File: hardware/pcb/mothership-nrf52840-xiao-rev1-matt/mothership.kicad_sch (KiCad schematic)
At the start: 42 parts, among them J1 HRO TYPE-C-31-M-12, J10 CONN_BATT, J11 Screw_Terminal_ADB_VCC, J2 USB_EXT_FFC_CABLE, J3 Screw_Terminal_ADB_SHIELD, J4 CONN_MATRIX_BOT_L, J5 CONN_MATRIX_BOT_R, J6 CONN_MATRIX_TOP_R, J7 CONN_MATRIX_TOP_L, J8 SPI, J9 EC11, Q1 AO3401A, Q2 FDC6305N, SW1 SW_SPDT_321, SW2 SW_SPST, U1 NCP361SN, U2 XIAO_nRF52840, U3 MCP23017x-x-SS, U4 MCP23017x-x-SS, U5 DT1452-02SO, U6 HY2115-LB9D

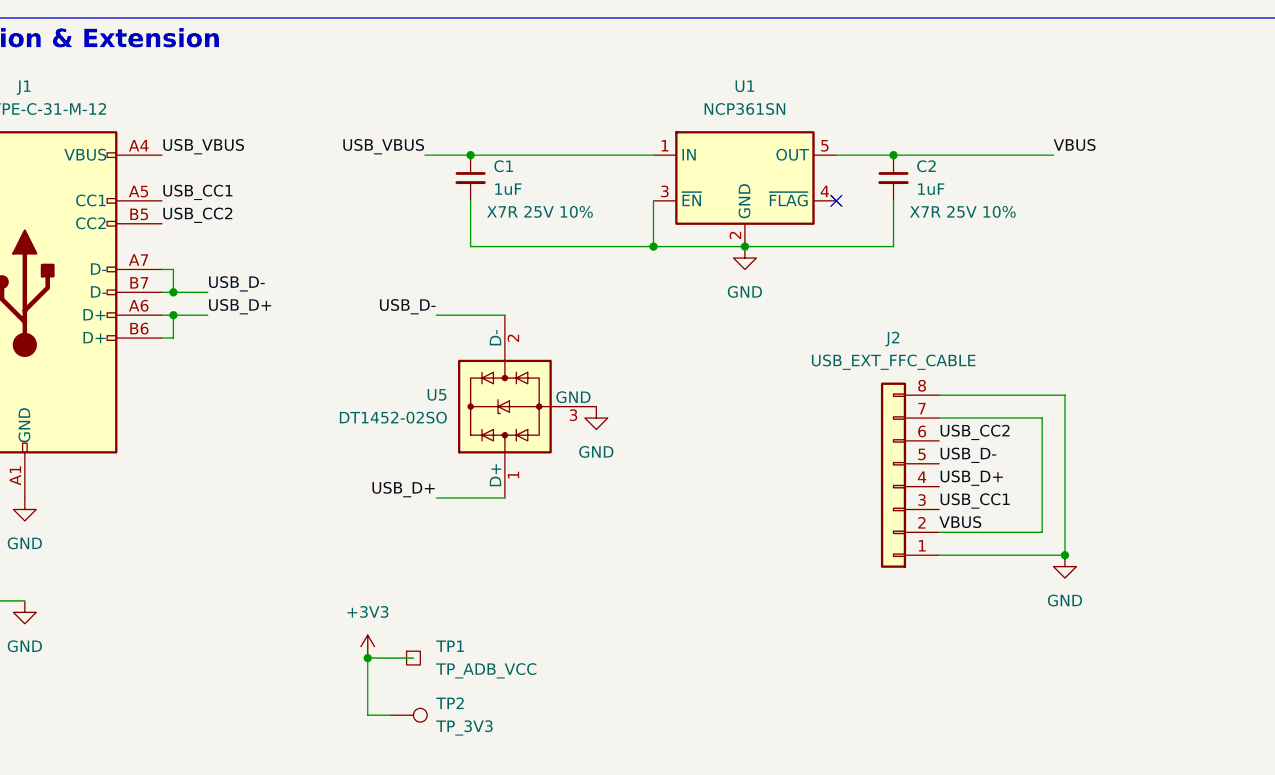
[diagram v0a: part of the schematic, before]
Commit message: sch: switch to use 4P flex adapter + 5.1k for CC lines
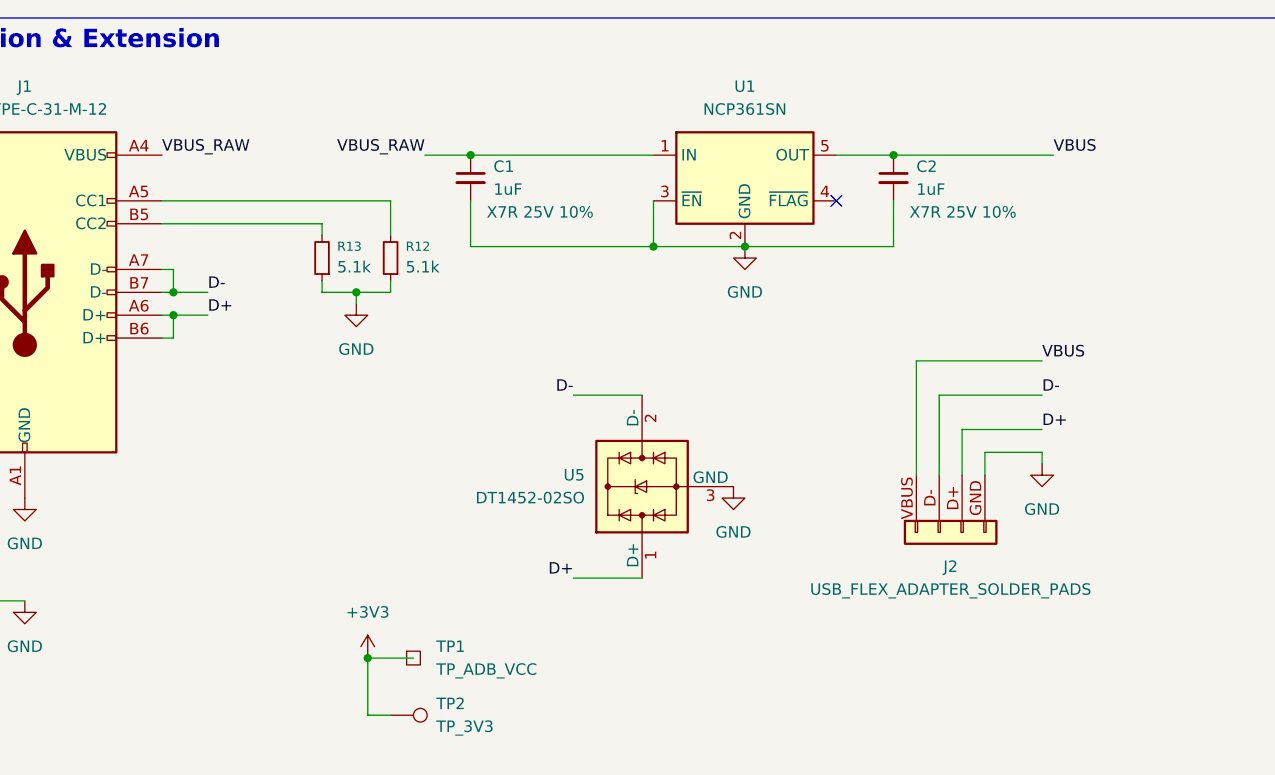
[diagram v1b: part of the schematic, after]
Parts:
- added R12, R13: 5.1k, A9M0330:Resistor_SMD__R_0603_1608Metric_Pad0.98x0.95mm_HandSolder, symbol A9M0330:R_Small
- J2: value USB_EXT_FFC_CABLE -> USB_FLEX_ADAPTER_SOLDER_PADS; symbol A9M0330:Conn_01x08 -> A9M0330:Conn_01x04_USB_FFC
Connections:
- net GND: now also J2.GND, R12.1, R13.1; no longer J2.1 (Pin_1), J2.8 (Pin_8)
- net USB_VBUS: no longer C1.1, J1.A4 (VBUS), J1.A9 (VBUS), J1.B4 (VBUS), J1.B9 (VBUS), U1.1 (IN)
- net VBUS: now also J2.VBUS; no longer J2.2 (Pin_2), J2.7 (Pin_7)
- net USB_CC1: no longer names the net of J1.A5 (CC1)
- net USB_CC1: now also R12.2; no longer J2.3 (Pin_3)
- net USB_CC2: no longer names the net of J1.B5 (CC2)
- net USB_CC2: now also R13.2; no longer J2.6 (Pin_6)
- net USB_D+ renamed D+
- net D+: now also J2.D+; no longer J2.4 (Pin_4)
- net USB_D- renamed D-
- net D-: now also J2.D-; no longer J2.5 (Pin_5)
- new net VBUS_RAW: C1.1, J1.A4 (VBUS), J1.A9 (VBUS), J1.B4 (VBUS), J1.B9 (VBUS), U1.1 (IN)
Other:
- moved on the sheet: U5

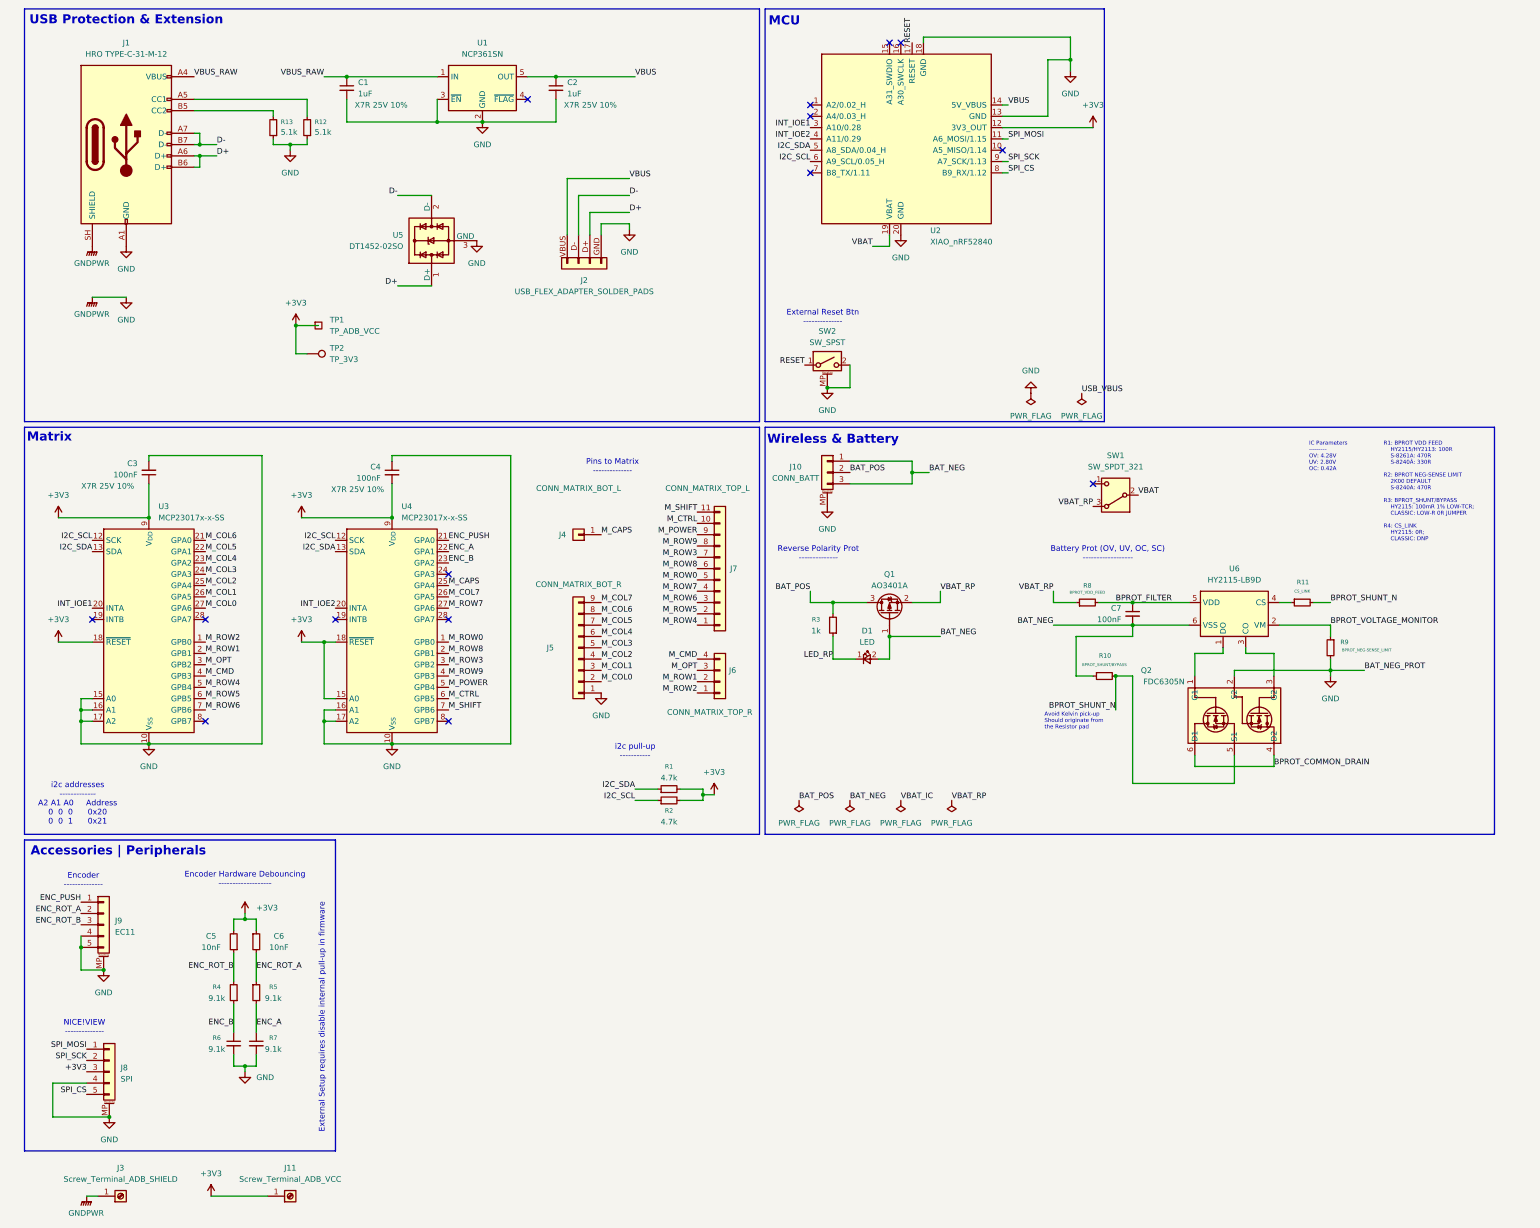
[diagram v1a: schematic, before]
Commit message: sch: switch to 4P usb flex + remove VBUS out from mcu
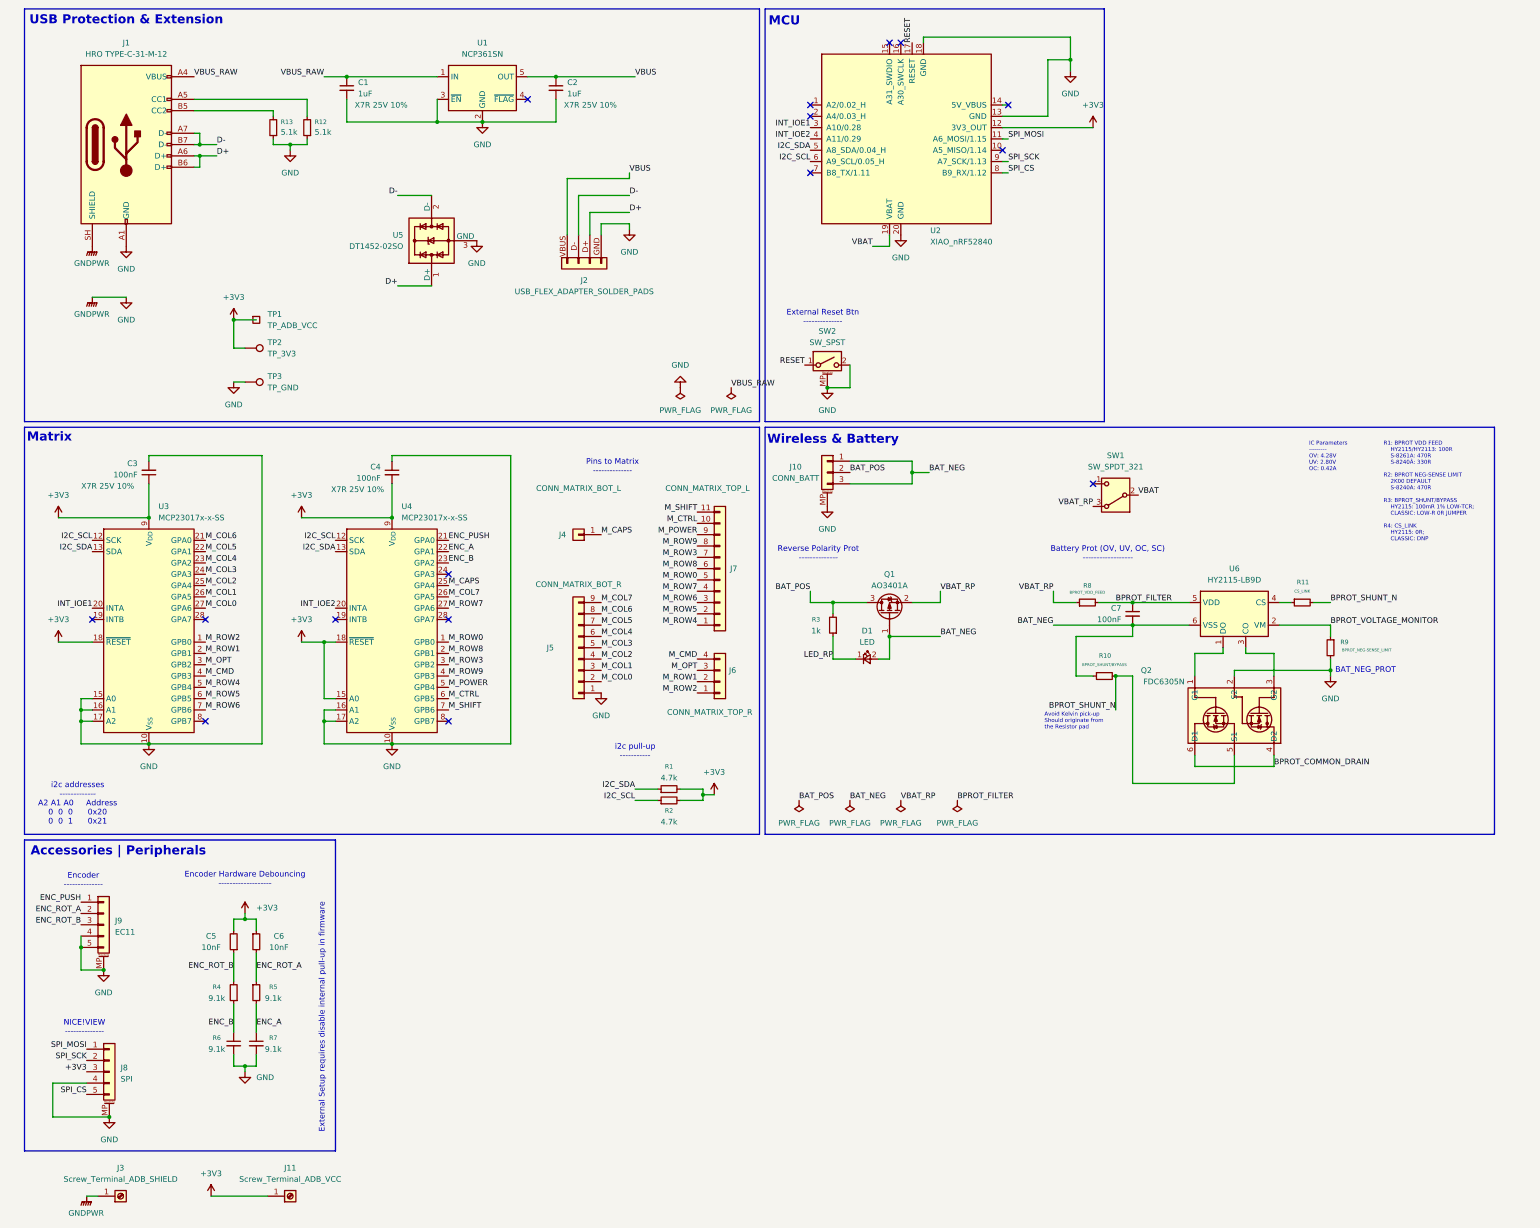
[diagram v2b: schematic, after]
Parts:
- added TP3: TP_GND, symbol A9M0330:TestPoint
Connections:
- net GND: now also TP3.1
- net VBUS: no longer U2.14 (5V_VBUS)
- no-connect marks 15 -> 16
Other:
- note added: "BAT_NEG_PROT"
- moved on the sheet: TP1, TP2

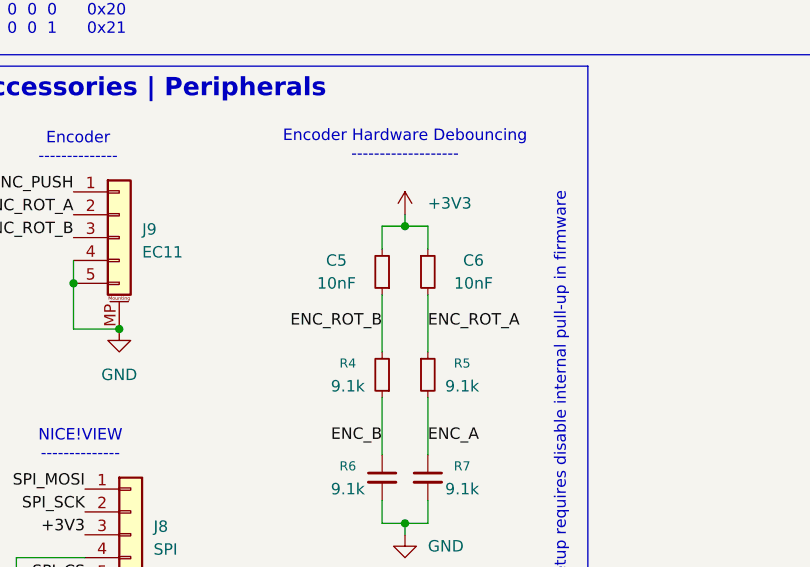
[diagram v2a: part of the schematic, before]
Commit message: sch: fix wrong value for EC11 cap hardwared debounce
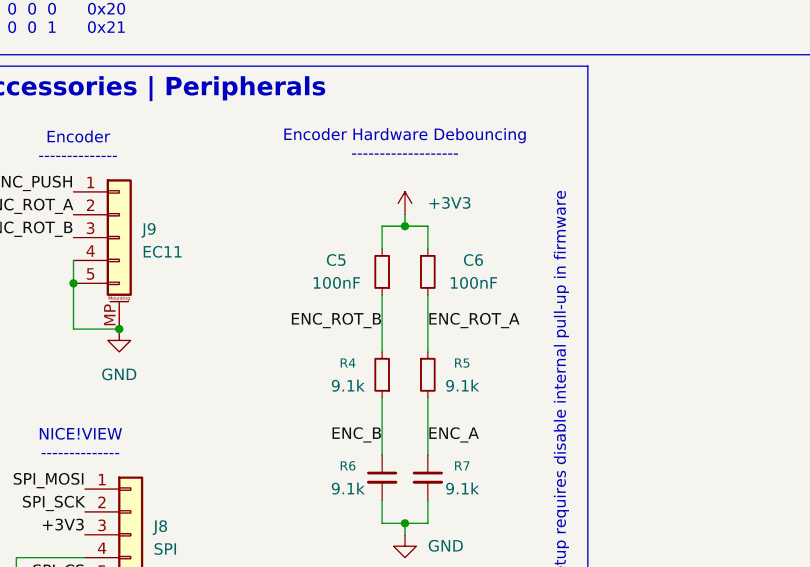
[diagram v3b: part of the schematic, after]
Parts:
- C5, C6: value 10nF -> 100nF
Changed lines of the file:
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@@
 			)
 		)
-		(property "Value" "10nF"
+		(property "Value" "100nF"
 			(at 54.6163 223.52 0)
 			(show_name no)
@@
 			)
 		)
-		(property "Value" "10nF"
+		(property "Value" "100nF"
 			(at 69.8436 223.52 0)
 			(show_name no)
